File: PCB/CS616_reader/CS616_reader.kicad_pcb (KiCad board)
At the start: 2 copper layers, 63.2 x 99.7 mm, 15 parts, among them J1 Conn_01x04_Socket, J2 Conn_01x04_Socket, J3 Conn_01x04_Socket, J4 Conn_01x04_Socket, J5 Conn_01x04_Socket, J6 Conn_01x04_Socket, J7 Conn_01x04_Socket, J8 Conn_01x04_Socket, J9 Conn_01x04_Socket, U1 CD4051B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

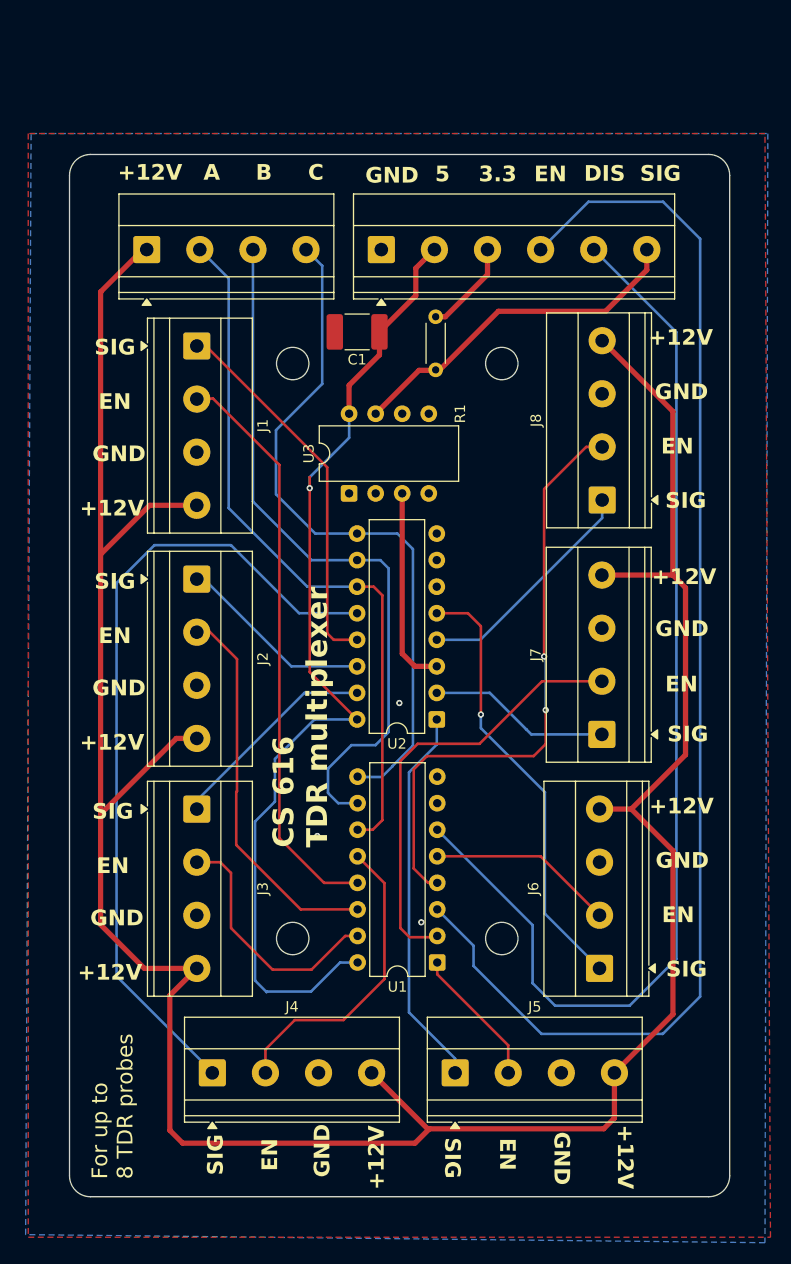
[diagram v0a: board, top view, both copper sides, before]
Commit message: addes small picture for pcb
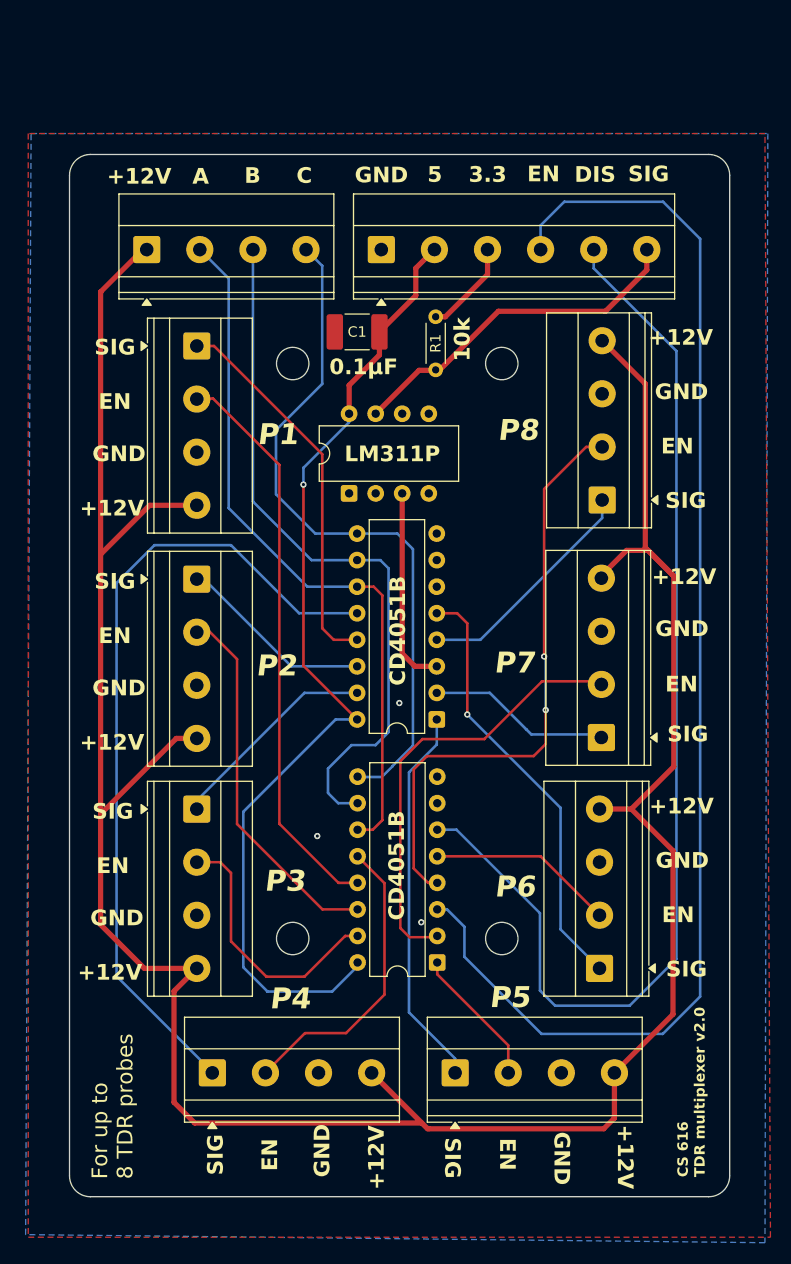
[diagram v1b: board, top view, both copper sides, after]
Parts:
- moved J7 0.30 mm to (139.5, 80.8)
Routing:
- net +12V: track 262.8 -> 259.6 mm
- net /ENABLE: track 123.8 -> 125.7 mm
- net /EN3: track 24.1 -> 25.4 mm
- net /EN2: track 37.0 -> 35.7 mm
- net /DISABLE: track 106.1 -> 107.2 mm
- net /EN1: track 55.5 -> 54.7 mm
- net +5V: track 95.7 -> 95.0 mm
- net /SIG6: track 42.2 -> 41.6 mm
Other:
- board text added: "0.1µF"
- board text added: "10k"
- board text added: "CD4051B"
- board text added: "CS 616 TDR multiplexer v2.0"
- board text added: "LM311P"
- board text added: "P1"
- board text added: "P2"
- board text added: "P3"
- board text added: "P4"
- board text added: "P5"
- board text added: "P6"
- board text added: "P7"
- board text added: "P8"
- board text removed: "CS 616 TDR multiplexer"

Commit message: Added logic level converter to pcb
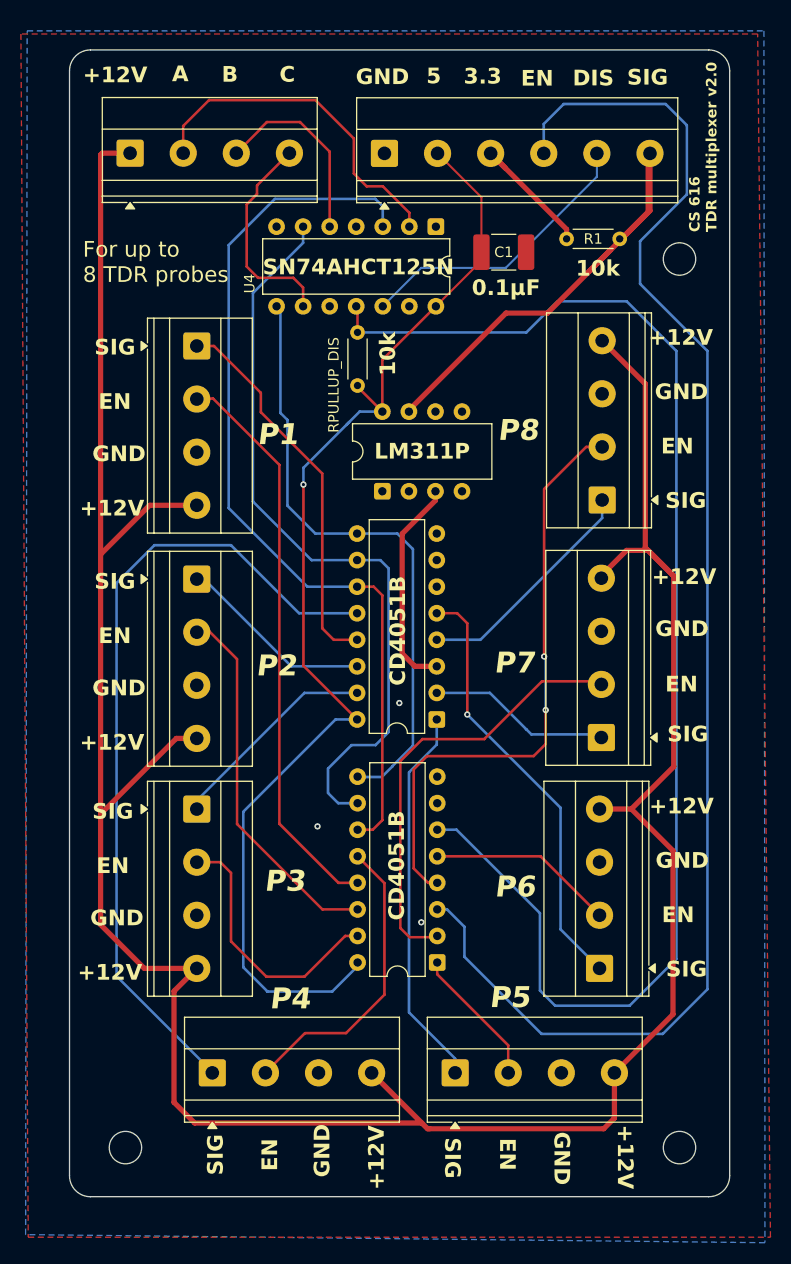
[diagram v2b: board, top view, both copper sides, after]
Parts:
- added RPULLUP_DIS: 10k, Resistor_THT:R_Axial_DIN0204_L3.6mm_D1.6mm_P5.08mm_Horizontal, F.Cu at (116.2, 42.0)
- added U4: 74AHCT125, Package_DIP:DIP-14_W7.62mm, F.Cu at (123.7, 31.9)
- R1: value 10kOhm -> 10k
- moved R1 21.6 mm to (141.3, 33.1), turned to 180 degrees
- moved C1 16.0 mm to (130.2, 34.4), turned to 0 degrees
- moved J9 9.36 mm to (94.4, 24.9)
- moved uC_Connector1 9.21 mm to (118.8, 24.9)
- moved U3 3.19 mm to (118.6, 57.2)
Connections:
- U1 pad 10: /Ctrl2 -> /CTRL2_5V
- U1 pad 11: /Ctrl1 -> /CTRL1_5V
- U1 pad 6: /DISABLE -> /DISABLE_5V
- U1 pad 9: /Ctrl3 -> /CTRL3_5V
- U2 pad 10: /Ctrl2 -> /CTRL2_5V
- U2 pad 11: /Ctrl1 -> /CTRL1_5V
- U2 pad 9: /Ctrl3 -> /CTRL3_5V
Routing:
- net /DISABLE_5V: track 0.00 -> 130.4 mm
- net /CTRL1_5V: track 0.00 -> 86.4 mm
- net /DISABLE: track 107.2 -> 27.9 mm
- net /CTRL2_5V: track 0.00 -> 72.4 mm
- net /CTRL3_5V: track 0.00 -> 58.6 mm
- net /Ctrl2: track 68.2 -> 18.5 mm
- net /Ctrl3: track 66.5 -> 20.6 mm
- net /Ctrl1: track 68.3 -> 33.0 mm
- net +5V: track 95.0 -> 112.9 mm
- net /SIGOUT: track 33.6 -> 50.0 mm
- net /ENABLE: track 125.7 -> 139.6 mm
- net +12V: track 259.6 -> 269.5 mm
- net +3.3V: track 9.08 -> 13.2 mm
- net /SIG: track 19.1 -> 20.7 mm
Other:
- board size 63.2 x 99.7 mm -> 63.2 x 109.7 mm
- board text added: "SN74AHCT125N"

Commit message: Improvements to pcb
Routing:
- net +5V: track 112.9 -> 104.7 mm
- net /CTRL1_5V: track 86.4 -> 87.8 mm
- net /SIG8: track 22.4 -> 21.5 mm
- net /CTRL3_5V: track 58.6 -> 58.0 mm
- net /DISABLE: track 27.9 -> 27.4 mm
